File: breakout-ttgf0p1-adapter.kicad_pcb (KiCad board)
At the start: 4 copper layers, 50 x 50 mm, 116 parts, among them J1 Conn_01x12, J2 Conn_02x08_Odd_Even, J3 DF12NB-60DS-0.5V_51, J4 Conn_02x08_Odd_Even, J5 DF12NB-50DS-0.5V_51, J6 Conn_02x08_Odd_Even, J8 Conn_02x08_Odd_Even, U1 AP2112K-3.3, U2 AP2112K-3.3, U4 24LC02

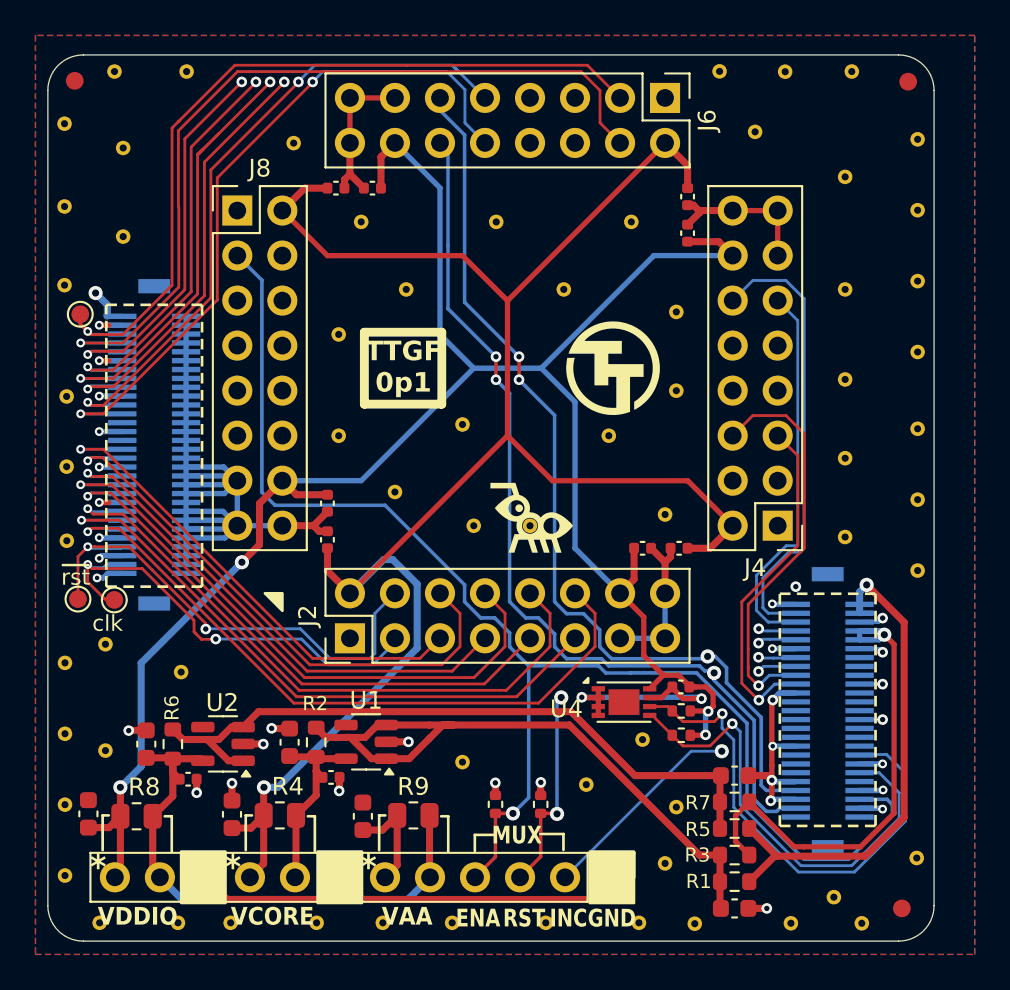
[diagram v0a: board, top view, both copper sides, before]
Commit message: replace THT headers with SMT ones & reroute
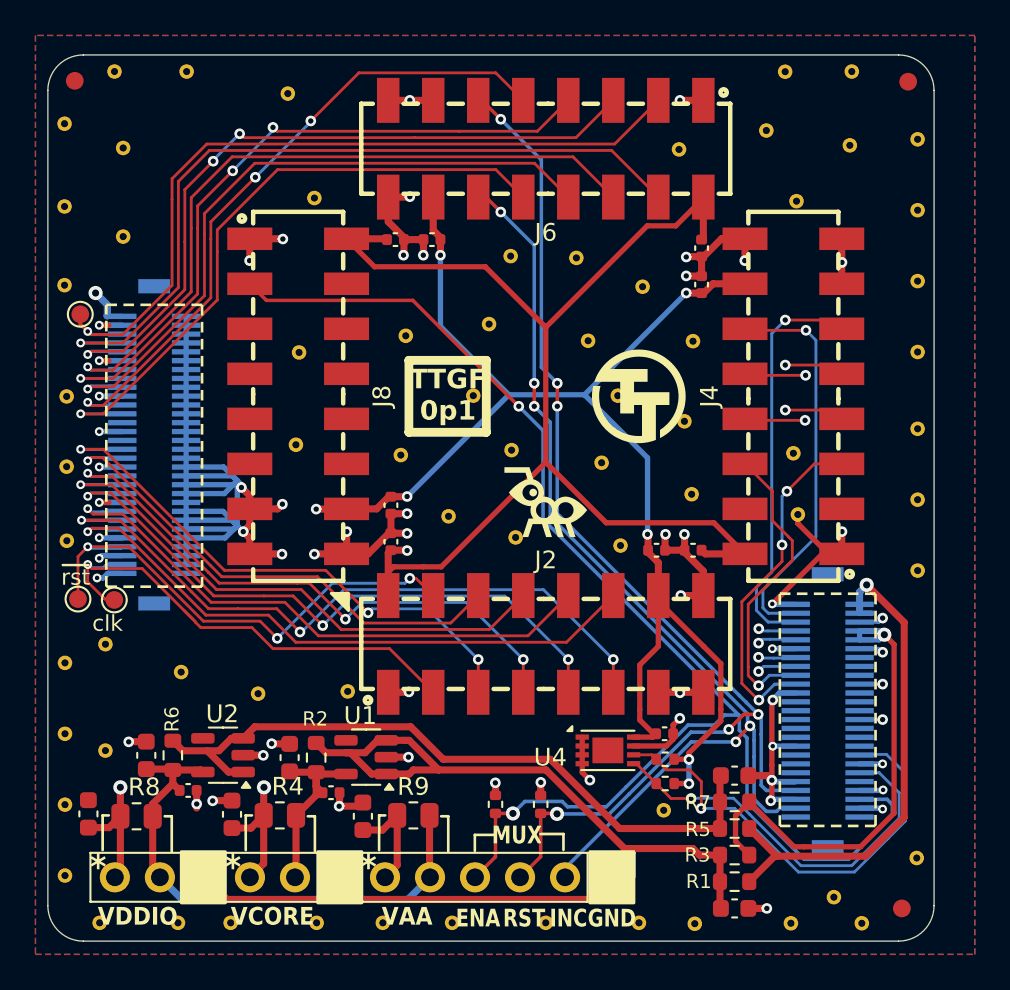
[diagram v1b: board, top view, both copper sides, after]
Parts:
- added STITCH01: StitchingVia-0.4mmDrill, flyingcarsfootprints:StitchingVia-0.4mmDrill, F.Cu at (155.1, 71.5)
- added STITCH01: StitchingVia-0.4mmDrill, flyingcarsfootprints:StitchingVia-0.4mmDrill, F.Cu at (155.3, 74.9)
- J2, J4, J6, J8: footprint Connector_PinHeader_2.54mm:PinHeader_2x08_P2.54mm_Vertical -> JLC2Kicad:HDR-SMD_16P-P2.54-V-F-R2-C8-LS7.2_H5.0
- moved STITCH01 33.3 mm to (126.5, 51.2)
- moved STITCH01 31.4 mm to (158.2, 54.1)
- moved STITCH01 30.9 mm to (129.9, 84.9)
- moved STITCH01 30.0 mm to (128.0, 57.1)
- moved STITCH01 28.7 mm to (139.1, 60.4)
- moved STITCH01 28.0 mm to (147.7, 91.6)
- moved STITCH01 27.2 mm to (124.9, 85.0)
- moved STITCH01 21.5 mm to (137.9, 64.2)
- moved STITCH01 21.4 mm to (127.2, 65.8)
- moved STITCH01 19.3 mm to (139.2, 71.3)
- moved STITCH01 18.2 mm to (146.6, 62.1)
- moved STITCH01 18.1 mm to (145.3, 76.7)
- moved STITCH01 17.7 mm to (139.4, 76.2)
- moved STITCH01 17.5 mm to (127.0, 71.0)
- moved STITCH01 17.3 mm to (148.6, 54.3)
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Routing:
- net VDD_{IO}: track 135.0 -> 107.5 mm, vias 4 -> 8
- net GND: track 161.5 -> 186.0 mm, vias 35 -> 59
- net VDD_{CORE}: track 115.8 -> 92.7 mm, vias 1 -> 2
- net /increment: track 69.3 -> 57.8 mm, vias 4 -> 5
- net /rst_n: track 73.4 -> 66.3 mm, vias 5 -> 6
- net /uout1: track 23.0 -> 17.2 mm
- net +3V3: track 100.6 -> 95.7 mm
- net /uin7: track 39.8 -> 35.6 mm
- net /uio7: track 40.0 -> 36.0 mm, vias 2 -> 1
- net /uin0: track 28.0 -> 31.9 mm, vias 1 -> 3
- net /uin5: track 36.9 -> 33.1 mm
- net /uio4: track 43.4 -> 39.6 mm, vias 2 -> 3
- net /uin6: track 35.6 -> 39.4 mm, vias 1 -> 3
- net /uin4: track 32.7 -> 36.5 mm, vias 1 -> 3
- net /uin2: track 29.8 -> 33.6 mm, vias 1 -> 3
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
